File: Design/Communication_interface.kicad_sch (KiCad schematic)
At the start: 59 parts, among them J1 CAN_JUM, J2 RS-485_1, J3 CAN-1, J4 CAN_JUM, J5 CAN-2, J6 RS-485_2, U5 ISO3082DW, U7 ISO3082DW

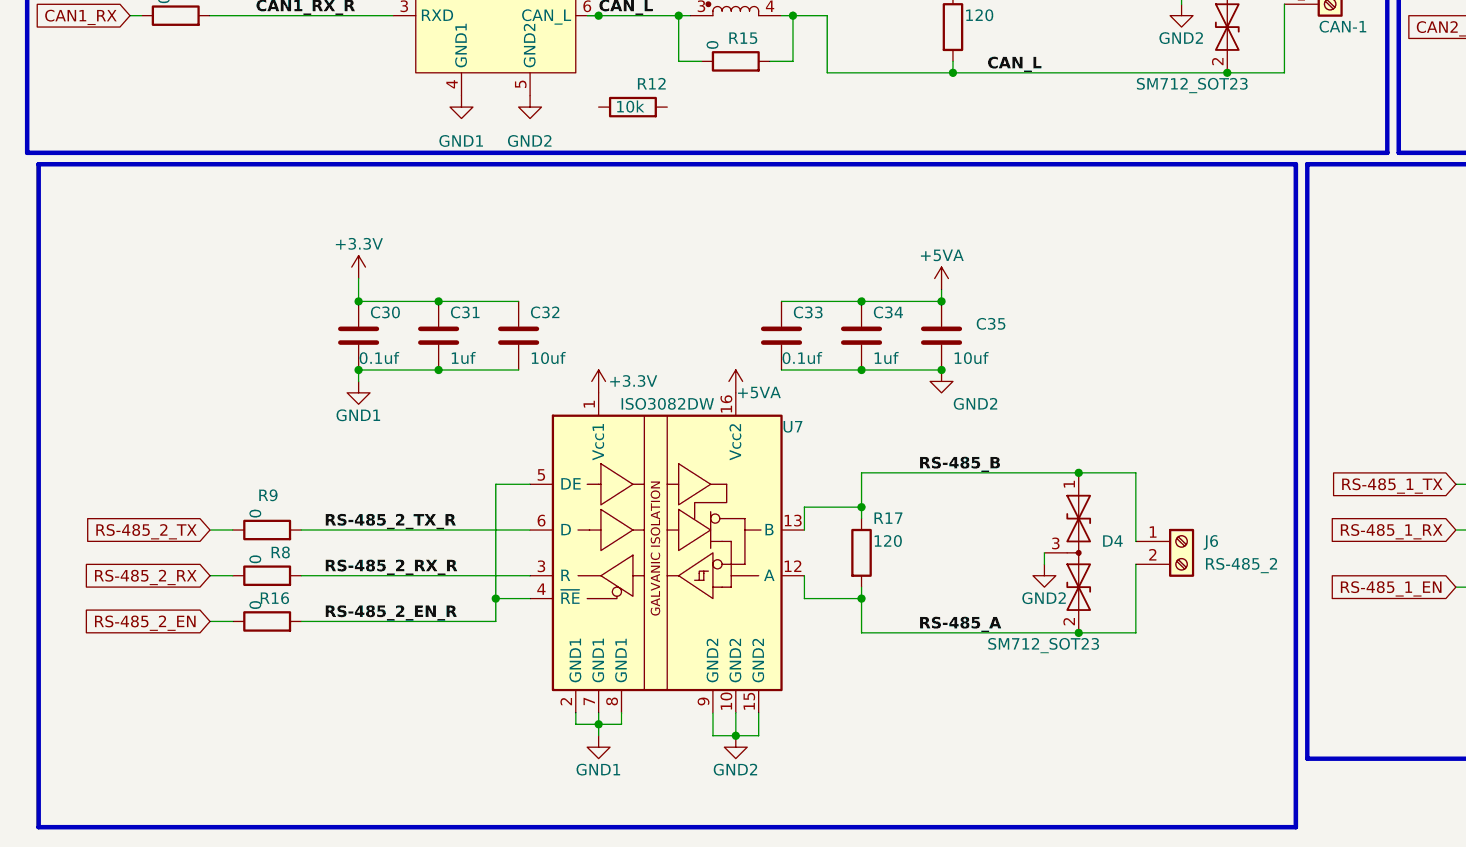
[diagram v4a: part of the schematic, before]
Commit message: LIN,I2C,SPI,SWD added , Power_stage created
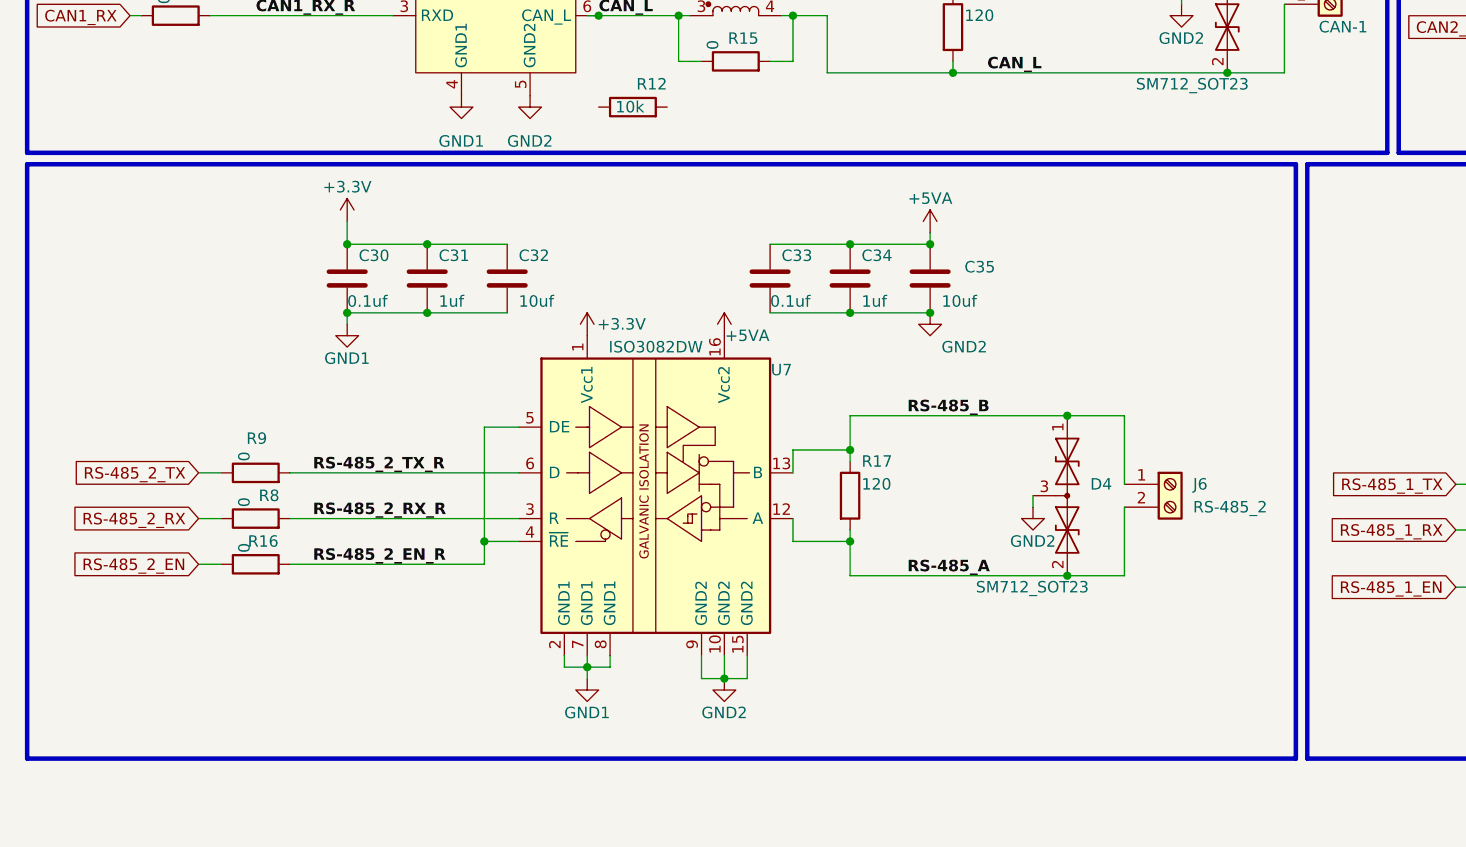
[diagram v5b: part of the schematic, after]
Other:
- moved on the sheet: C30, C31, C32, C33, C34, C35, D4, J6, R16, R17, R8, R9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

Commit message: Setup Power supply
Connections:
- net CAN_H: now also D2.1 (A1), J4.2 (Pin_2), J5.1 (Pin_1), L2.2, R19.2

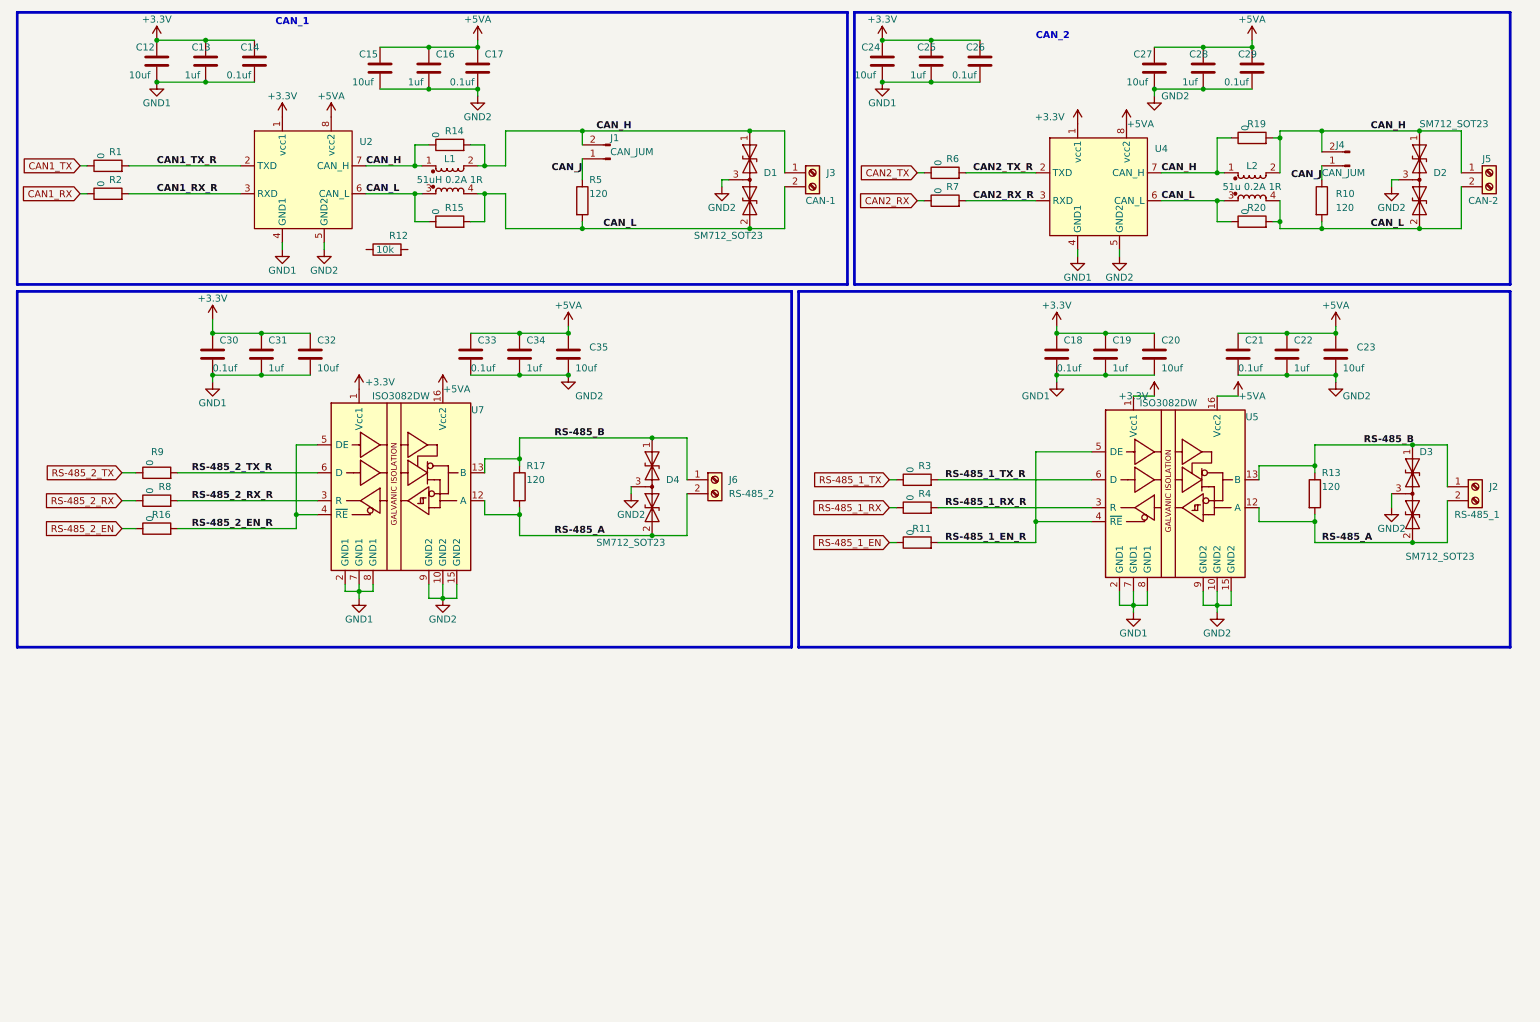
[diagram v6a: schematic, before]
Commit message: Footprints added to all componenets
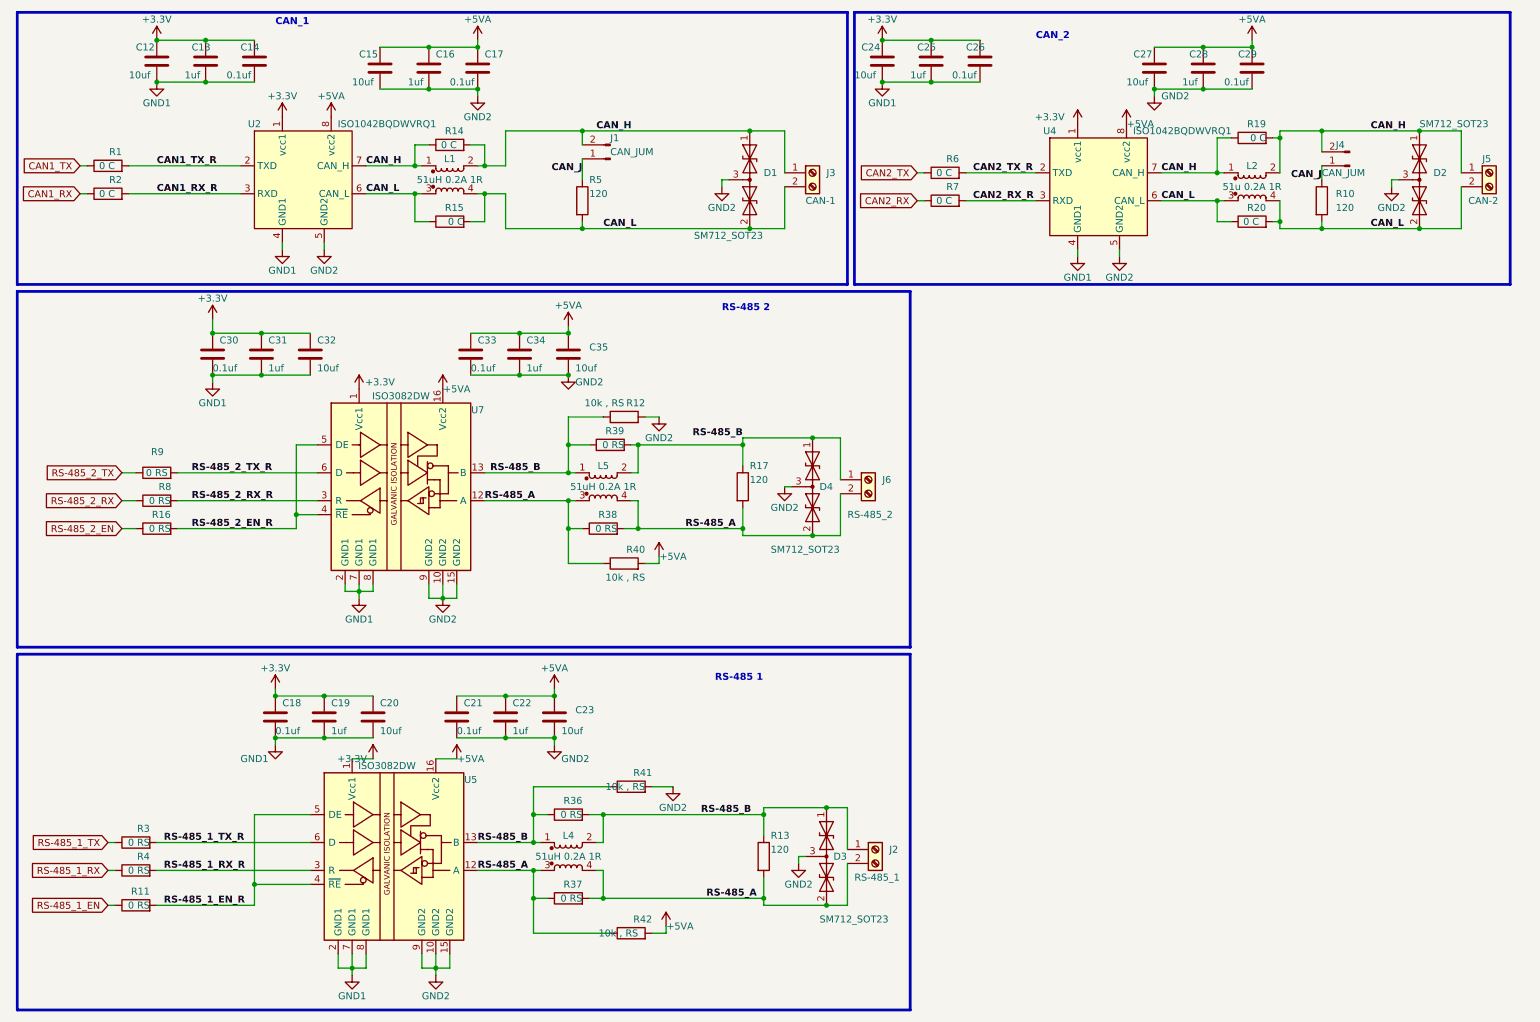
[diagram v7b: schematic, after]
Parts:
- added L4, L5: 51uH 0.2A 1R, symbol Device:L_Coupled
- added R36, R37, R38, R39: 0 RS, Resistor_SMD:R_0603_1608Metric_Pad0.98x0.95mm_HandSolder, symbol Device:R
- added R40, R41, R42: 10k , RS, Resistor_SMD:R_0805_2012Metric_Pad1.20x1.40mm_HandSolder, symbol Device:R
- C12, C15, C20, C23, C24, C27, C32, C35: footprint (none) -> Capacitor_SMD:C_0805_2012Metric_Pad1.18x1.45mm_HandSolder
- C13, C14, C16, C17, C18, C19, C21, C22, C25, C26, C28, C29, C30, C31, C33, C34: footprint (none) -> Capacitor_SMD:C_0603_1608Metric_Pad1.08x0.95mm_HandSolder
- J1, J4: footprint (none) -> Connector_PinHeader_2.54mm:PinHeader_1x02_P2.54mm_Vertical
- R1, R14, R15, R19, R2, R20, R6, R7: value 0 -> 0 C; footprint (none) -> Resistor_SMD:R_0603_1608Metric_Pad0.98x0.95mm_HandSolder
- R10, R13, R17, R5: footprint (none) -> Resistor_SMD:R_0805_2012Metric_Pad1.20x1.40mm_HandSolder
- R11, R16, R3, R4, R8, R9: value 0 -> 0 RS; footprint (none) -> Resistor_SMD:R_0603_1608Metric_Pad0.98x0.95mm_HandSolder
- R12: value 10k -> 10k , RS; footprint (none) -> Resistor_SMD:R_0805_2012Metric_Pad1.20x1.40mm_HandSolder
- U2, U4: value ~ -> ISO1042BQDWVRQ1
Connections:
- net +5VA: now also R40.2, R42.2
- net GND2: now also R12.2, R41.2
- net RS-485_A: now also L4.3, L4.4, L5.3, L5.4, R37.1, R37.2, R38.1, R38.2, R40.1, R42.1
- net RS-485_B: now also R12.1, L4.1, L4.2, L5.1, L5.2, R36.1, R36.2, R39.1, R39.2, R41.1
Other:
- note added: "RS-485 1"
- note added: "RS-485 2"
- moved on the sheet: C18, C19, C20, C21, C22, C23, D3, D4, J2, J6, R11, R12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

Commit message: CMC component name added
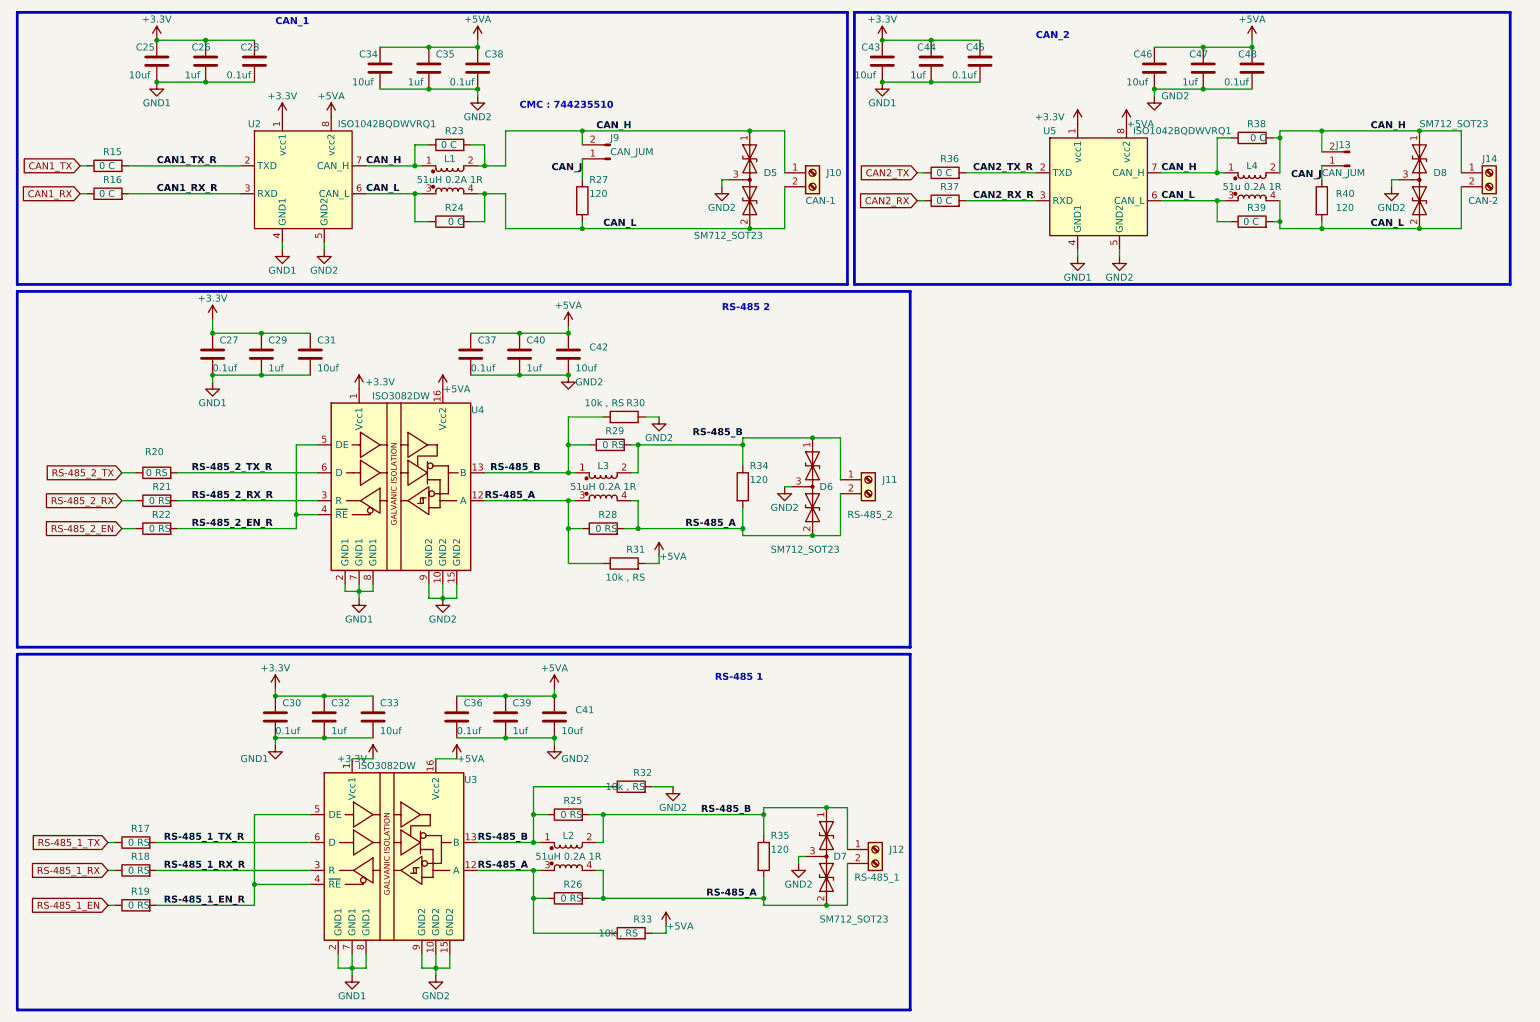
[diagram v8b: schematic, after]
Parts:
- renumbered C12 to C25, C13 to C26, C30 to C27, C14 to C28, C31 to C29, C18 to C30, C32 to C31, C19 to C32, C20 to C33, C15 to C34, C16 to C35, C21 to C36, C33 to C37, C17 to C38, C22 to C39, C34 to C40, C23 to C41, C35 to C42, C24 to C43, C25 to C44, C26 to C45, C27 to C46, C28 to C47, C29 to C48, D1 to D5, D4 to D6, D3 to D7, D2 to D8, J3 to J10, J6 to J11, J2 to J12, J4 to J13, J5 to J14, J1 to J9, L4 to L2, L5 to L3, L2 to L4, R1 to R15, R2 to R16, R3 to R17, R4 to R18, R11 to R19, R9 to R20, R8 to R21, R16 to R22, R14 to R23, R15 to R24, R36 to R25, R37 to R26, R5 to R27, R38 to R28, R39 to R29, R12 to R30, R40 to R31, R41 to R32, R42 to R33, R17 to R34, R13 to R35, R6 to R36, R7 to R37, R19 to R38, R20 to R39, R10 to R40, U5 to U3, U7 to U4, U4 to U5
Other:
- note added: "CMC : 744235510"
